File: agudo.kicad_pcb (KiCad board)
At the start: 2 copper layers, 28.8 x 54 mm, 49 parts, among them J1 Stomp_Connector, J2 Power_Connector, J3 Power_TOP, Q1 MMBF5457, Q2 MMBF5457, U1 TL072, U2 TL072

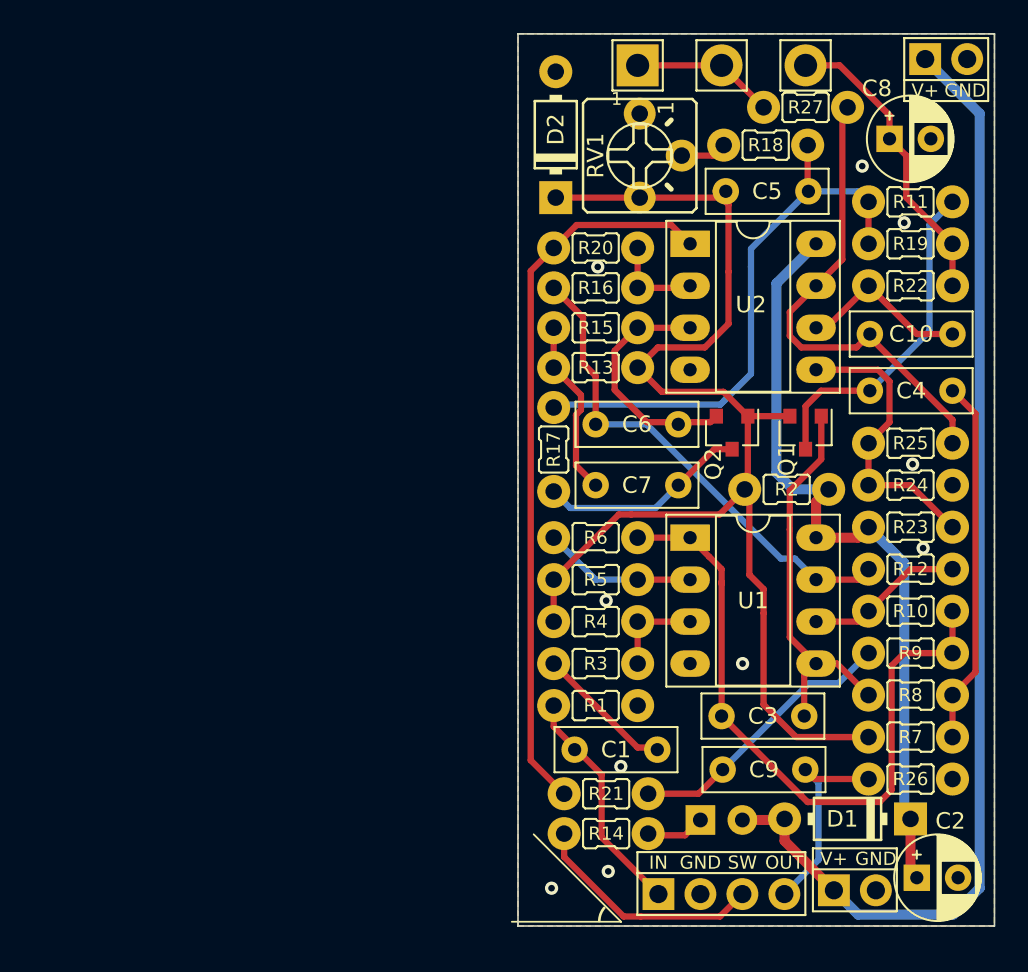
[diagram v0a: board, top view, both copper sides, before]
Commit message: v0.2: SMD board, fully connected but bit of a spaghetti mess
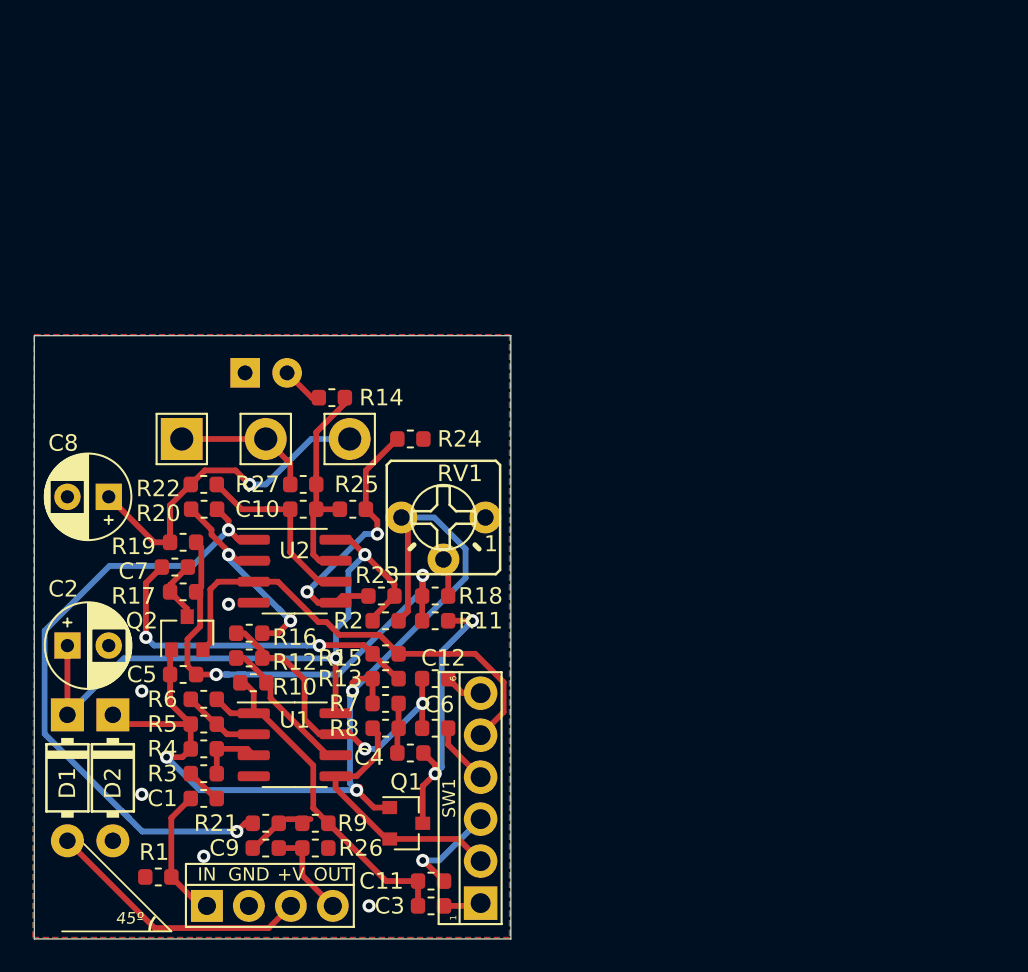
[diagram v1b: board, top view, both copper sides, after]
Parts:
- removed J2: Power_Connector, rockola_kicad_footprints:Power_Header_2pin
- removed J3: Power_TOP, rockola_kicad_footprints:Power_Header_2pin_TOP
- added C11: 10n, Capacitor_SMD:C_0603_1608Metric, F.Cu at (82.8, 130.0)
- added C12: 100n, Capacitor_SMD:C_0603_1608Metric, F.Cu at (83.0, 117.8)
- added SW1: Vibe, switches:DPDT.WIRE, F.Cu at (85.8, 125.0)
- C1, C10, C3, C4, C5, C6, C7, C9: footprint rockola_kicad_footprints:C_Box_7.2_2.5 -> Capacitor_SMD:C_0603_1608Metric
- J1: footprint rockola_kicad_footprints:Stomp_4pin -> rockola_kicad_footprints:Stomp_4pin_Power_No_LED
- R1, R10, R11, R12, R13, R14, R15, R16, R17, R18, R19, R2, R20, R21, R22, R23, R24, R25, R26, R27, R3, R4, R5, R6, R7, R8, R9: footprint rockola_kicad_footprints:R_0.125W_5mm -> Resistor_SMD:R_0603_1608Metric
- U1, U2: footprint Package_DIP:DIP-8_W7.62mm_Socket_LongPads -> Package_SO:SOIC-8_3.9x4.9mm_P1.27mm
- moved C2 53.3 mm to (60.8, 115.8)
- moved C8 52.0 mm to (63.2, 106.8), turned to 180 degrees
- moved R19 47.6 mm to (67.8, 109.5), turned to 180 degrees
- moved D1 47.3 mm to (60.8, 123.8), turned to -90 degrees
- moved D2 47.2 mm to (63.5, 123.8), turned to -90 degrees
- moved R22 44.4 mm to (69.0, 106.0), turned to 0 degrees
- moved C5 44.0 mm to (67.8, 117.5)
- moved C10 40.7 mm to (75.0, 107.5), turned to 0 degrees
- moved R12 40.4 mm to (71.8, 116.5), turned to 0 degrees
- moved R10 40.0 mm to (72.0, 118.0), turned to 0 degrees
- moved C4 39.5 mm to (81.5, 122.2), turned to 0 degrees
- moved D3 38.6 mm to (71.5, 99.2)
- moved R11 38.3 mm to (83.0, 114.2)
- moved R27 38.0 mm to (75.0, 106.0)
- moved R9 37.5 mm to (75.8, 126.5), turned to 0 degrees
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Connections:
- net Net-(C6-Pad1) renamed U1B_OUT
- C2 pad 1: +9V -> VCC
- C3 pad 1: Net-(C3-Pad1) -> U1A_OUT
- C9 pad 1: Net-(C9-Pad1) -> Net-(R21-Pad2)
- D1 pad 1: +9V -> VCC
- D1 pad 2: VIN -> +9V
- D3 pad 1: Net-(D3-Pad1) -> GND
- D3 pad 2: VIN -> Net-(R14-Pad2)
- J1 pad 3: LED- -> +9V
- Q1 pad D: Net-(C3-Pad2) -> Net-(C5-Pad1)
- Q1 pad S: Net-(C5-Pad1) -> U1B_IN
- Q2 pad S: Net-(C6-Pad2) -> U2A_IN
- R10 pad 1: Net-(C3-Pad1) -> U1A_OUT
- R14 pad 1: LED- -> Net-(C10-Pad2)
- R14 pad 2: Net-(D3-Pad1) -> Net-(R14-Pad2)
- R15 pad 2: Net-(C6-Pad2) -> U2A_IN
- R2 pad 1: +9V -> VCC
- R21 pad 2: Net-(C9-Pad1) -> Net-(R21-Pad2)
- R23 pad 1: +9V -> VCC
- R6 pad 2: Net-(C3-Pad1) -> U1A_OUT
- R8 pad 2: Net-(C3-Pad2) -> U1B_IN
- R9 pad 1: Net-(C3-Pad1) -> Net-(R21-Pad2)
- R9 pad 2: Net-(C9-Pad1) -> U1A_OUT
- U1 pad 1: Net-(C3-Pad1) -> U1A_OUT
- U1 pad 5: Net-(C3-Pad2) -> U1B_IN
- U1 pad 8: +9V -> VCC
- U2 pad 3: Net-(C6-Pad2) -> U2A_IN
- U2 pad 8: +9V -> VCC
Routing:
- net VIN: track 69.5 -> 0.00 mm
- net Net-(C3-Pad1): track 41.6 -> 0.00 mm
- net VCC: track 0.00 -> 39.6 mm, vias 0 -> 2
- net +9V: track 48.0 -> 16.3 mm
- net U2A_IN: track 0.00 -> 28.1 mm
- net U1A_OUT: track 0.00 -> 21.8 mm
- net Net-(C3-Pad2): track 23.9 -> 2.28 mm
- net Net-(C4-Pad1): track 22.1 -> 3.03 mm
- net Net-(C5-Pad1): track 77.6 -> 60.5 mm, vias 0 -> 3
- net Net-(C9-Pad1): track 17.0 -> 0.00 mm
- net U1B_IN: track 0.00 -> 16.2 mm
- net Net-(C10-Pad2): track 29.4 -> 13.7 mm
- net LED-: track 14.2 -> 0.00 mm
- net Net-(C6-Pad2): track 14.6 -> 3.77 mm
- net U1B_OUT: track 30.0 -> 19.2 mm, vias 0 -> 2
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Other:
- board size 28.8 x 54 mm -> 28.8 x 36.5 mm
- net class Default removed
- board text added: "${REVISION} ${DATE}"
- board text added: "${TITLE}"
- board text added: "${URL}"
- board text added: "45º"
- board text removed: "1"
- board text removed: "Agudo"
- board text removed: "github.com/rockola/agudo"
- board text removed: "v0.1 2020-04-27"
